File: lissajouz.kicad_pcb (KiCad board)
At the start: 2 copper layers, 100 x 100 mm, 107 parts, among them J1 Barrel_Jack, Q1 BC557, Q10 2N7000, Q2 BC557, Q3 2N7000, Q4 BC557, Q5 BC557, Q6 2N7000, Q7 2N7000, Q8 2N7000, Q9 2N7000, U1 LM324, U2 LM324, U3 LM324

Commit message: kinda final-ish UI layout
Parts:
- added J2: AudioJack3, Connector_Audio:Jack_3.5mm_CUI_SJ1-3535NG_Horizontal, B.Cu at (64.7, 55.2)
- added R26: 100k, Resistor_SMD:R_0805_2012Metric_Pad1.20x1.40mm_HandSolder, F.Cu at (3.35, 46.4)
- added R62: 100k, Resistor_SMD:R_0805_2012Metric_Pad1.20x1.40mm_HandSolder, F.Cu at (3.35, 49.4)
- added R63: 1k, Resistor_SMD:R_0805_2012Metric_Pad1.20x1.40mm_HandSolder, F.Cu at (3.35, 52.3)
- added R64: 1k, Resistor_SMD:R_0805_2012Metric_Pad1.20x1.40mm_HandSolder, F.Cu at (3.35, 55.3)
- added R65: 1k, Resistor_SMD:R_0805_2012Metric_Pad1.20x1.40mm_HandSolder, F.Cu at (3.35, 58.2)
- added R66: 2.2k, Resistor_SMD:R_0805_2012Metric_Pad1.20x1.40mm_HandSolder, F.Cu at (3.35, 61.2)
- added R67: 4.7k, Resistor_SMD:R_0805_2012Metric_Pad1.20x1.40mm_HandSolder, F.Cu at (3.35, 64.1)
- added R68: 4.7k, Resistor_SMD:R_0805_2012Metric_Pad1.20x1.40mm_HandSolder, F.Cu at (3.35, 67.1)
- added R69: 1Meg, Resistor_SMD:R_0805_2012Metric_Pad1.20x1.40mm_HandSolder, F.Cu at (3.35, 70.0)
- added RV12: 10k, Potentiometer_THT:Potentiometer_Alpha_RD901F-40-00D_Single_Vertical, F.Cu at (115.5, 69.7)
- added RV13: 10k, Potentiometer_THT:Potentiometer_Alpha_RD901F-40-00D_Single_Vertical, F.Cu at (69.7, 120.5)
- added RV14: 10k, Potentiometer_THT:Potentiometer_Alpha_RD901F-40-00D_Single_Vertical, F.Cu at (103.7, 106.5)
- added SW1: r=0, footprints:switch8x8, F.Cu at (90.1, 89.4)
- added SW2: r=0, footprints:switch8x8, F.Cu at (100.0, 79.5)
- J1: footprint Connector_BarrelJack:BarrelJack_SwitchcraftConxall_RAPC10U_Horizontal -> footprints:myBarrelJack; moved to B.Cu
- moved J1 209.1 mm to (142.5, 73.8), turned to 90 degrees
- moved RV6 171.2 mm to (66.7, 136.5), turned to 180 degrees
- moved D3 155.0 mm to (143.6, 122.9), turned to -135 degrees
- moved R36 149.7 mm to (69.7, 91.5), turned to 180 degrees
- moved U1 144.0 mm to (78.9, 126.9)
- moved U2 143.3 mm to (111.8, 103.7)
- moved U3 137.5 mm to (126.2, 88.5), turned to 90 degrees
- moved R34 118.2 mm to (69.7, 105.5), turned to 180 degrees
- moved D1 59.0 mm to (54.9, 63.9)
- moved RV11 51.8 mm to (60.8, 77.5), turned to 90 degrees
- moved R15 13.5 mm to (100.5, 69.7)
- moved R17 13.5 mm to (86.5, 69.7)
- moved RV10 13.0 mm to (72.5, 60.8)
- moved RV9 8.06 mm to (113.6, 96.6)
- moved RV7 1.41 mm to (86.7, 113.6)
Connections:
- R40 pad 1: syncphase -> sync_phase
- RV5 pad 3: GNDREF -> Net-(R63-Pad2)
- RV6 pad 3: GNDREF -> Net-(R64-Pad2)
- RV7 pad 3: GNDREF -> Net-(R65-Pad2)
- RV8 pad 3: GNDREF -> Net-(R66-Pad2)
- RV9 pad 1: VCC -> Net-(R67-Pad1)
- RV9 pad 3: GNDREF -> Net-(R68-Pad2)
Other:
- board text added: "X axis"
- board text added: "Y axis"
- board text added: "coarse"
- board text added: "fine"
- board text added: "freq"
- board text added: "gain"
- board text added: "low frequency oscillator"
- board text added: "phase"
- board text added: "power"
- board text added: "shape"
- board text added: "slant"
- board text added: "sync"

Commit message: all components positioned
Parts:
- C1, C10, C11, C12, C13, C14, C15, C2, C3, C4, C5, C6, C7, C8, C9, R1, R10, R11, R12, R13, R14, R16, R18, R19, R2, R20, R21, R22, R23, R24, R25, R26, R27, R28, R29, R3, R30, R31, R32, R33, R35, R37, R38, R39, R4, R40, R41, R42, R43, R44, R45, R46, R47, R48, R49, R5, R50, R51, R52, R53, R54, R55, R56, R57, R58, R59, R6, R60, R61, R62, R63, R64, R65, R66, R67, R68, R69, R7, R8, R9: moved to B.Cu
- D3: footprint Diode_THT:D_5W_P5.08mm_Vertical_AnodeUp -> Diode_THT:D_5W_P12.70mm_Horizontal
- moved R5 196.8 mm to (144.0, 84.8), turned to 180 degrees
- moved R18 191.0 mm to (143.5, 87.5)
- moved R14 189.8 mm to (140.2, 86.8), turned to -90 degrees
- moved R11 189.2 mm to (137.0, 86.8), turned to -90 degrees
- moved R61 187.4 mm to (146.8, 126.5), turned to 90 degrees
- moved R1 186.4 mm to (132.8, 75.2), turned to 90 degrees
- moved R10 186.1 mm to (134.5, 92.5), turned to 180 degrees
- moved R6 184.9 mm to (130.5, 92.5), turned to 180 degrees
- moved R2 184.8 mm to (132.8, 71.2), turned to 90 degrees
- moved R9 183.9 mm to (119.2, 129.2), turned to 135 degrees
- moved R41 182.7 mm to (139.0, 109.5), turned to 135 degrees
- moved R45 180.7 mm to (129.2, 119.2), turned to 135 degrees
- moved R28 176.0 mm to (109.5, 139.0), turned to 135 degrees
- moved R12 174.8 mm to (124.2, 82.2), turned to 180 degrees
- moved R8 174.7 mm to (124.2, 80.0), turned to 180 degrees
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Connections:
- C1 pad 1: GNDREF -> GND
- C12 pad 1: GNDREF -> GND
- C14 pad 1: GNDREF -> GND
- C2 pad 1: /tri_x -> /tri_y
- C3 pad 1: /tri_x -> /tri_y
- C4 pad 1: GNDREF -> GND
- C5 pad 1: GNDREF -> GND
- C6 pad 1: /tri_y -> /tri_x
- C7 pad 1: /tri_y -> /tri_x
- C8 pad 1: GNDREF -> GND
- C9 pad 1: GNDREF -> GND
- J2 pad S: GNDREF -> GND
- Q10 pad 1: GNDREF -> GND
- Q3 pad 1: GNDREF -> GND
- Q6 pad 1: GNDREF -> GND
- Q9 pad 1: GNDREF -> GND
- R11 pad 1: GNDREF -> GND
- R14 pad 1: GNDREF -> GND
- R14 pad 2: sync_x -> sync_y
- R18 pad 1: sync_x -> sync_y
- R23 pad 1: out_y -> out_x
- R25 pad 1: V_yfreq -> V_xfreq
- R26 pad 1: V_xfreq_fine -> V_yfreq_fine
- R28 pad 1: lfo_syncfreq -> lfo_xfreq
- R30 pad 1: GNDREF -> GND
- R33 pad 1: GNDREF -> GND
- R33 pad 2: sync_y -> sync_x
- R37 pad 1: sync_y -> sync_x
- R41 pad 1: lfo_syncfreq -> lfo_syncphase
- R47 pad 1: GNDREF -> GND
- R49 pad 1: GNDREF -> GND
- R49 pad 2: Net-(U3B-+) -> Net-(U3D-+)
- R5 pad 1: out_x -> out_y
- R51 pad 1: Net-(U3B-+) -> Net-(U3D-+)
- R54 pad 1: GNDREF -> GND
- R56 pad 1: GNDREF -> GND
- R56 pad 2: Net-(U3D-+) -> Net-(U3B-+)
- R57 pad 1: Net-(U3D-+) -> Net-(U3B-+)
- R62 pad 1: V_yfreq_fine -> V_xfreq_fine
- R63 pad 1: GNDREF -> GND
- R64 pad 1: GNDREF -> GND
- R65 pad 1: GNDREF -> GND
- R66 pad 1: GNDREF -> GND
- R7 pad 1: V_xfreq -> V_yfreq
- R9 pad 1: lfo_syncfreq -> lfo_yfreq
- RV1 pad 2: lfo_syncfreq -> lfo_xfreq
- RV1 pad 3: GNDREF -> GND
- RV10 pad 3: GNDREF -> GND
- RV11 pad 3: GNDREF -> GND
- RV12 pad 3: GNDREF -> GND
- RV13 pad 3: GNDREF -> GND
- RV2 pad 2: lfo_syncfreq -> lfo_yfreq
- RV2 pad 3: GNDREF -> GND
- RV3 pad 3: GNDREF -> GND
- RV4 pad 2: lfo_syncfreq -> lfo_syncphase
- RV4 pad 3: GNDREF -> GND
- U1 pad 1: /tri_x -> /tri_y
- U1 pad 13: GNDREF -> GND
- U1 pad 14: GNDREF -> GND
- U1 pad 5: sync_x -> sync_y
- U1 pad 6: /tri_x -> /tri_y
- U1 pad 8: out_x -> out_y
- U2 pad 1: /tri_y -> /tri_x
- U2 pad 5: sync_y -> sync_x
- U2 pad 6: /tri_y -> /tri_x
- U2 pad 8: out_y -> out_x
- U3 pad 13: /lfo_tri -> /sync_tri
- U3 pad 14: Net-(Q10-G) -> Net-(Q9-G)
- U3 pad 6: /sync_tri -> /lfo_tri
- U3 pad 7: Net-(Q9-G) -> Net-(Q10-G)
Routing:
- net GND: track 0.00 -> 60.4 mm
- net VEE: track 0.00 -> 19.2 mm
- net Net-(U1D-+): track 0.00 -> 10.0 mm
- net VCC: track 0.00 -> 9.15 mm

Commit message: minimal routing
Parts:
- renumbered REF** to HOLE1, REF** to HOLE2, REF** to HOLE3, REF** to HOLE4
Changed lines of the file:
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@@
 		(descr "Mounting Hole 3.2mm, no annular, M3")
 		(tags "mounting hole 3.2mm no annular m3")
-		(property "Reference" "REF**"
+		(property "Reference" "HOLE1"
 			(at 0 -4.2 0)
 			(layer "F.SilkS")
@@
 		(descr "Mounting Hole 3.2mm, no annular, M3")
 		(tags "mounting hole 3.2mm no annular m3")
-		(property "Reference" "REF**"
+		(property "Reference" "HOLE2"
 			(at 0 -4.2 0)
 			(layer "F.SilkS")
@@
 		(descr "Mounting Hole 3.2mm, no annular, M3")
 		(tags "mounting hole 3.2mm no annular m3")
-		(property "Reference" "REF**"
+		(property "Reference" "HOLE3"
 			(at 0 -4.2 0)
 			(layer "F.SilkS")
@@
 		(descr "Mounting Hole 3.2mm, no annular, M3")
 		(tags "mounting hole 3.2mm no annular m3")
-		(property "Reference" "REF**"
+		(property "Reference" "HOLE4"
 			(at 0 -4.2 0)
 			(layer "F.SilkS")

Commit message: board adjustments
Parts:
- R15, R17, R34, R36, RV1, RV12, RV13, RV14, RV2, RV3, RV4, RV5, RV6, RV7, RV8, RV9: footprint Potentiometer_THT:Potentiometer_Alpha_RD901F-40-00D_Single_Vertical -> footprints:my_poti_Potentiometer_Alpha_RD901F-40-00D_Single_Vertical
- moved D2 6.57 mm to (139.0, 127.0), turned to 45 degrees
- moved R61 5.13 mm to (143.0, 123.0), turned to 135 degrees
- moved D3 1.00 mm to (145.2, 113.5)
- moved J1 0.99 mm to (143.5, 73.8)
- moved J2 0.94 mm to (64.7, 54.2)
- moved R26 0.50 mm to (67.0, 116.8)
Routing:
- net GND: track 60.4 -> 445.6 mm, vias 0 -> 2
- net VEE: track 19.2 -> 383.3 mm, vias 0 -> 16
- net VCC: track 9.15 -> 305.8 mm, vias 0 -> 3
- net Net-(R24-Pad1): track 0.00 -> 136.8 mm
- net Net-(R10-Pad2): track 0.00 -> 126.8 mm, vias 0 -> 2
- net /lfo_tri: track 0.00 -> 112.2 mm
- net out_y: track 0.00 -> 103.2 mm
- net Net-(U2D-+): track 0.00 -> 101.4 mm, vias 0 -> 5
- net out_x: track 0.00 -> 83.1 mm
- net Net-(Q3-G): track 0.00 -> 73.2 mm
- net sync_x: track 0.00 -> 71.9 mm
- net Net-(U2A--): track 0.00 -> 70.9 mm
- net Net-(C10-Pad2): track 0.00 -> 70.6 mm, vias 0 -> 1
- net Net-(R43-Pad1): track 0.00 -> 69.7 mm, vias 0 -> 4
- net Net-(U1A--): track 0.00 -> 63.5 mm, vias 0 -> 1
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- added copper zone on B.Cu, net VEE
- added copper zone on F.Cu, net VEE
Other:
- board text added: "JLCJLCJLCJLC"

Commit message: frontplate++
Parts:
- added R70: 10k, Resistor_SMD:R_0805_2012Metric_Pad1.20x1.40mm_HandSolder, B.Cu at (106.0, 72.5)
- added R71: 10k, Resistor_SMD:R_0805_2012Metric_Pad1.20x1.40mm_HandSolder, B.Cu at (67.0, 102.0)
- moved R63 11.8 mm to (128.0, 66.8), turned to 0 degrees
- moved R64 9.89 mm to (64.0, 137.8), turned to 90 degrees
- moved C6 8.75 mm to (67.0, 98.0), turned to -90 degrees
- moved R3 5.52 mm to (122.2, 72.5)
- moved R4 5.52 mm to (118.0, 72.5)
- moved R32 5.02 mm to (66.8, 87.8)
- moved R13 5.00 mm to (91.5, 73.0)
- moved R38 4.76 mm to (67.0, 106.8), turned to 90 degrees
- moved R66 3.54 mm to (133.2, 135.8), turned to -45 degrees
- moved C2 1.50 mm to (101.8, 72.5), turned to 0 degrees
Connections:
- R15 pad 1: Net-(C2-Pad2) -> Net-(R15-Pad1)
- R34 pad 1: Net-(C6-Pad2) -> Net-(R34-Pad1)
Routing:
- net VEE: track 383.3 -> 274.0 mm, vias 16 -> 1
- net Net-(R24-Pad1): track 136.8 -> 174.1 mm
- net /lfo_tri: track 112.2 -> 83.0 mm
- net VCC: track 305.8 -> 330.2 mm, vias 3 -> 0
- net Net-(U2D-+): track 101.4 -> 119.9 mm, vias 5 -> 1
- net /tri_x: track 60.1 -> 73.4 mm
- net Net-(Q8-D): track 47.0 -> 34.4 mm
- net Net-(R10-Pad2): track 126.8 -> 115.5 mm
- net out_y: track 103.2 -> 93.3 mm
- net GND: track 445.6 -> 436.4 mm, vias 2 -> 0
- net Net-(R43-Pad1): track 69.7 -> 60.6 mm, vias 4 -> 2
- net Net-(R65-Pad2): track 2.24 -> 10.9 mm
- net Net-(U1A--): track 63.5 -> 55.6 mm
- net Net-(R67-Pad1): track 2.72 -> 10.7 mm
- net /tri_y: track 60.8 -> 54.2 mm
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
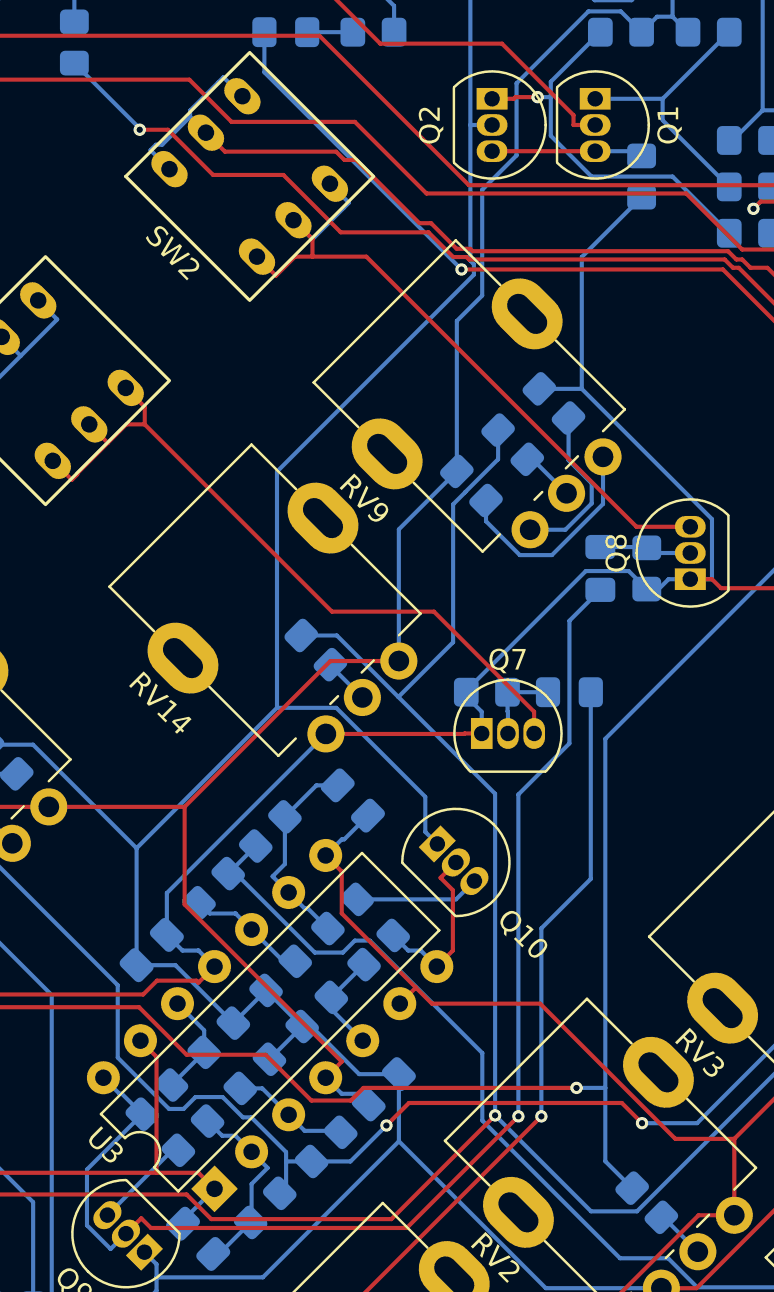
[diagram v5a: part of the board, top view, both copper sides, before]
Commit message: Fine-tuning and fix switch footprint
- fine-tune slant poti range
- reduce x/y freq lfo when not synced
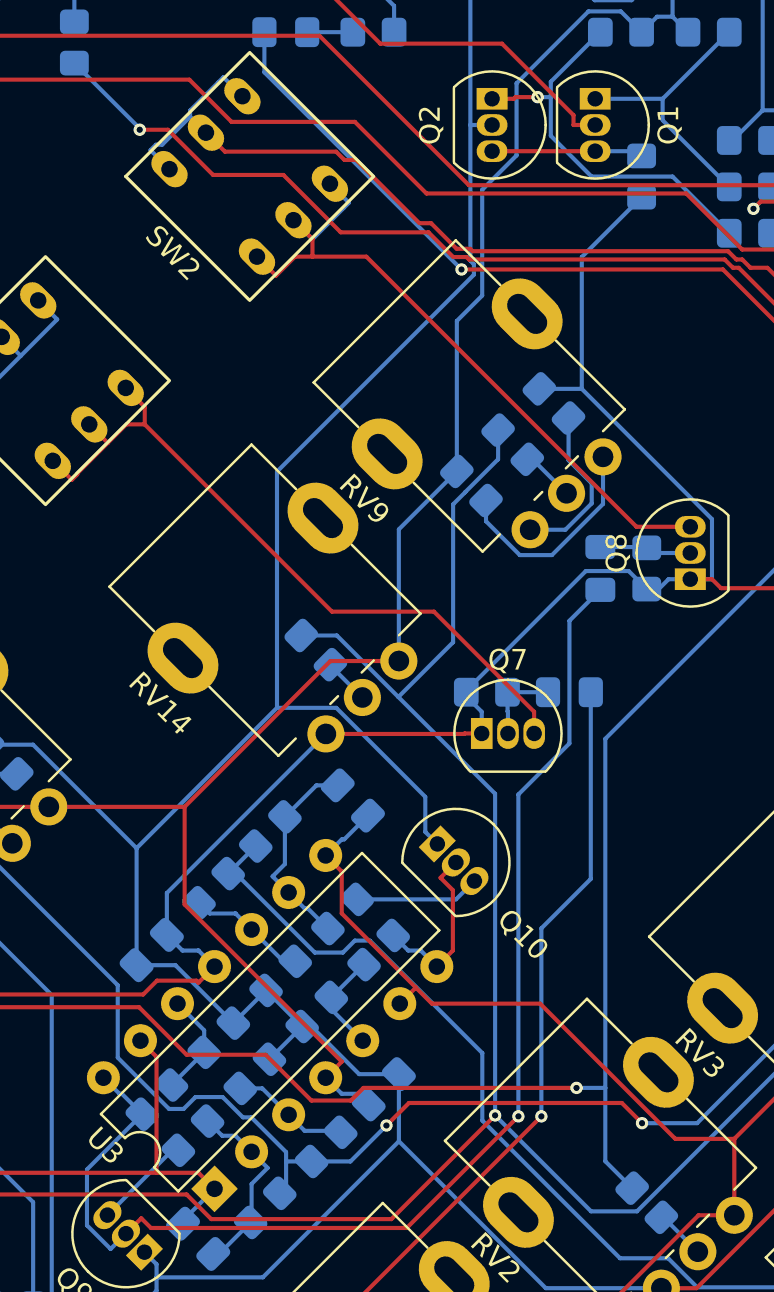
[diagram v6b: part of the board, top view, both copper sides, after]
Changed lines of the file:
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@@
 		(fp_arc
 			(start 1.27 -2.6)
-			(mid 3.672088 -0.994977)
+			(mid 3.672087 -0.994977)
 			(end 3.108478 1.838478)
 			(stroke
@@
 		(fp_arc
 			(start 1.27 -2.48)
-			(mid 3.561222 -0.949055)
+			(mid 3.561221 -0.949055)
 			(end 3.023625 1.753625)
 			(stroke
@@
 		(fp_arc
 			(start 1.27 -2.6)
-			(mid 3.672088 -0.994977)
+			(mid 3.672087 -0.994977)
 			(end 3.108478 1.838478)
 			(stroke
@@
 		(fp_arc
 			(start 1.27 -2.48)
-			(mid 3.561222 -0.949055)
+			(mid 3.561221 -0.949055)
 			(end 3.023625 1.753625)
 			(stroke
@@
 		(fp_arc
 			(start 4.810001 -1.33)
-			(mid 3.81 -0.33)
+			(mid 3.81 -0.330001)
 			(end 2.81 -1.33)
 			(stroke

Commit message: Fix bugs in PCB
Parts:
- added D4: 1N4148, Diode_THT:D_DO-35_SOD27_P7.62mm_Horizontal, F.Cu at (119.2, 141.8)
- added R72: 10k, Resistor_SMD:R_0805_2012Metric_Pad1.20x1.40mm_HandSolder, B.Cu at (136.2, 132.8)
- added R73: 4.7k, Resistor_SMD:R_0805_2012Metric_Pad1.20x1.40mm_HandSolder, B.Cu at (127.3, 121.3)
- added R74: 100k, Resistor_SMD:R_0805_2012Metric_Pad1.20x1.40mm_HandSolder, B.Cu at (90.5, 88.0)
- added R75: 100k, Resistor_SMD:R_0805_2012Metric_Pad1.20x1.40mm_HandSolder, B.Cu at (100.5, 78.0)
- added R76: 220k, Resistor_SMD:R_0805_2012Metric_Pad1.20x1.40mm_HandSolder, B.Cu at (104.2, 67.2)
- added R77: 220k, Resistor_SMD:R_0805_2012Metric_Pad1.20x1.40mm_HandSolder, B.Cu at (67.0, 101.8)
- added REF**: OSHW-Logo2_9.8x8mm_SilkScreen, Symbol:OSHW-Logo2_9.8x8mm_SilkScreen, F.Cu at (97.5, 145.2)
- added wf: LOGO, footprints:windfisch_smaller, F.Cu at (78.9, 79.3)
- D3: value D -> 1N4148; footprint Diode_THT:D_5W_P12.70mm_Horizontal -> Diode_THT:D_DO-35_SOD27_P7.62mm_Horizontal
- Q1, Q2, Q4, Q5: value BC557 -> BC547
- R15: renamed from R17; value 47k -> 100k
- R17: renamed from R15; value 100k -> 50k
- R26: renamed from R62; value 100k -> 470k
- R34: renamed from R36; value 47k -> 100k
- R36: renamed from R34; value 100k -> 50k
- R60: value 1k -> 10k
- R61: value 470 -> 4.7k
- R62: renamed from R26; value 100k -> 470k
- R66: value 2.2k -> 1k
- SW1, SW2: value r=0 -> SW_DPDT_x2
- moved Q3 43.4 mm to (122.3, 87.8)
- moved D3 36.4 mm to (119.2, 139.0), turned to 0 degrees
- moved R32 15.2 mm to (72.8, 101.8)
- moved C6 14.2 mm to (67.0, 83.8)
- moved R38 14.2 mm to (67.0, 92.5)
- moved R71 14.2 mm to (67.0, 87.8)
- moved R19 14.0 mm to (88.0, 67.5)
- moved C2 14.0 mm to (87.8, 72.2)
- moved R70 14.0 mm to (92.0, 72.2)
- moved R13 14.0 mm to (105.5, 73.0)
- moved R69 14.0 mm to (112.8, 92.3)
- moved R40 14.0 mm to (102.8, 102.3)
- moved R67 14.0 mm to (100.8, 104.3)
- moved R68 14.0 mm to (104.8, 100.3)
- moved R66 0.71 mm to (132.8, 136.2)
- renumbered R7 to R25, R59 to R58, R58 to R59, R64 to R63, R63 to R64, R25 to R7, RV11 to RV10, RV10 to RV11, RV13 to RV12, RV12 to RV13, RV9 to RV14, RV6 to RV5, RV5 to RV6, RV14 to RV9
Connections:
- D3 pad 1: VEE -> Net-(D3-K)
- R15 pad 1: Net-(R13-Pad1) -> Net-(R15-Pad1)
- R15 pad 2: Net-(Q3-D) -> Net-(Q1-B)
- R17 pad 1: Net-(R15-Pad1) -> Net-(R13-Pad1)
- R17 pad 2: Net-(Q1-B) -> Net-(Q3-D)
- R25 pad 1: V_yfreq -> V_xfreq
- R25 pad 2: Net-(R10-Pad2) -> Net-(R24-Pad1)
- R26 pad 1: V_xfreq_fine -> V_yfreq_fine
- R26 pad 2: Net-(R24-Pad1) -> Net-(R10-Pad2)
- R34 pad 1: Net-(R32-Pad1) -> Net-(R34-Pad1)
- R34 pad 2: Net-(Q6-D) -> Net-(Q4-B)
- R36 pad 1: Net-(R34-Pad1) -> Net-(R32-Pad1)
- R36 pad 2: Net-(Q4-B) -> Net-(Q6-D)
- R58 pad 1: Net-(J2-PadT) -> Net-(J2-PadR)
- R59 pad 1: Net-(J2-PadR) -> Net-(J2-PadT)
- R62 pad 1: V_yfreq_fine -> V_xfreq_fine
- R62 pad 2: Net-(R10-Pad2) -> Net-(R24-Pad1)
- R7 pad 1: V_xfreq -> V_yfreq
- R7 pad 2: Net-(R24-Pad1) -> Net-(R10-Pad2)
- RV1 pad 1: /lfo_tri -> Net-(SW1B-B)
- RV10 pad 1: out_y -> out_x
- RV11 pad 1: out_x -> out_y
- RV12 pad 2: V_yfreq_fine -> V_xfreq_fine
- RV13 pad 2: V_xfreq_fine -> V_yfreq_fine
- RV14 pad 1: Net-(R67-Pad1) -> VCC
- RV14 pad 2: sync_phase -> sync_phase_fine
- RV14 pad 3: Net-(R68-Pad2) -> VEE
- RV2 pad 1: /lfo_tri -> Net-(SW2B-B)
- RV5 pad 2: V_yfreq -> V_xfreq
- RV6 pad 2: V_xfreq -> V_yfreq
- RV8 pad 1: VCC -> Net-(R72-Pad1)
- RV9 pad 1: VCC -> Net-(R67-Pad1)
- RV9 pad 2: sync_phase_fine -> sync_phase
- RV9 pad 3: VEE -> Net-(R68-Pad2)
- SW1 pad 1: Net-(Q7-D) -> unconnected-(SW1A-A-Pad1)
- SW1 pad 2: sync_x -> Net-(Q7-D)
- SW2 pad 1: Net-(Q8-D) -> unconnected-(SW2A-A-Pad1)
- SW2 pad 2: sync_y -> Net-(Q8-D)
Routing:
- net Net-(R24-Pad1): track 174.1 -> 86.6 mm
- net Net-(SW1B-B): track 0.00 -> 71.0 mm
- net Net-(SW2B-B): track 0.00 -> 70.1 mm, vias 0 -> 1
- net Net-(Q3-G): track 73.3 -> 26.9 mm
- net GND: track 436.4 -> 468.5 mm
- net Net-(U2A--): track 76.3 -> 46.1 mm
- net /lfo_tri: track 83.0 -> 112.5 mm
- net Net-(R10-Pad2): track 115.5 -> 86.4 mm, vias 2 -> 0
- net Net-(Q3-D): track 6.88 -> 33.2 mm
- net VCC: track 330.2 -> 348.0 mm, vias 0 -> 2
- net Net-(Q1-B): track 19.8 -> 34.0 mm
- net /tri_y: track 54.2 -> 68.4 mm
- net Net-(U1A--): track 55.6 -> 42.3 mm
- net Net-(D2-K): track 5.64 -> 18.9 mm
- net sync_y: track 61.3 -> 49.0 mm
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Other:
- board text added: "9-20V"
- board text added: "https://github.com/Windfisch/lissajouz"
- board text added: "prefer 12V"
- board text added: "rev02"
